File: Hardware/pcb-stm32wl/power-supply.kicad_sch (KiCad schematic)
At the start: 32 parts, among them J2 JST-PH, Q1 PMV32UP,215, Q3 PMV32UP,215, U11 MIC5365-3.3YD5, U12 TPS22917DBV, U8 MAX1837ETT50+T, U9 WE-TPC_5828

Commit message: review session 2
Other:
- note added: "ADD IN ANOTHER BATTERY"
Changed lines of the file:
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@@
-	)
-	(rectangle
-		(start 15.875 140.335)
-		(end 94.615 197.485)
-		(stroke
-			(width 0.508)
-			(type default)
-		)
-		(fill
-			(type none)
-		)
 	)
 	(rectangle
@@
 			)
 		)
+	)
+	(text "ADD IN ANOTHER BATTERY"
+		(exclude_from_sim no)
+		(at 130.048 18.034 0)
+		(effects
+			(font
+				(size 1.4986 1.4986)
+				(color 0 255 0 1)
+			)
+		)

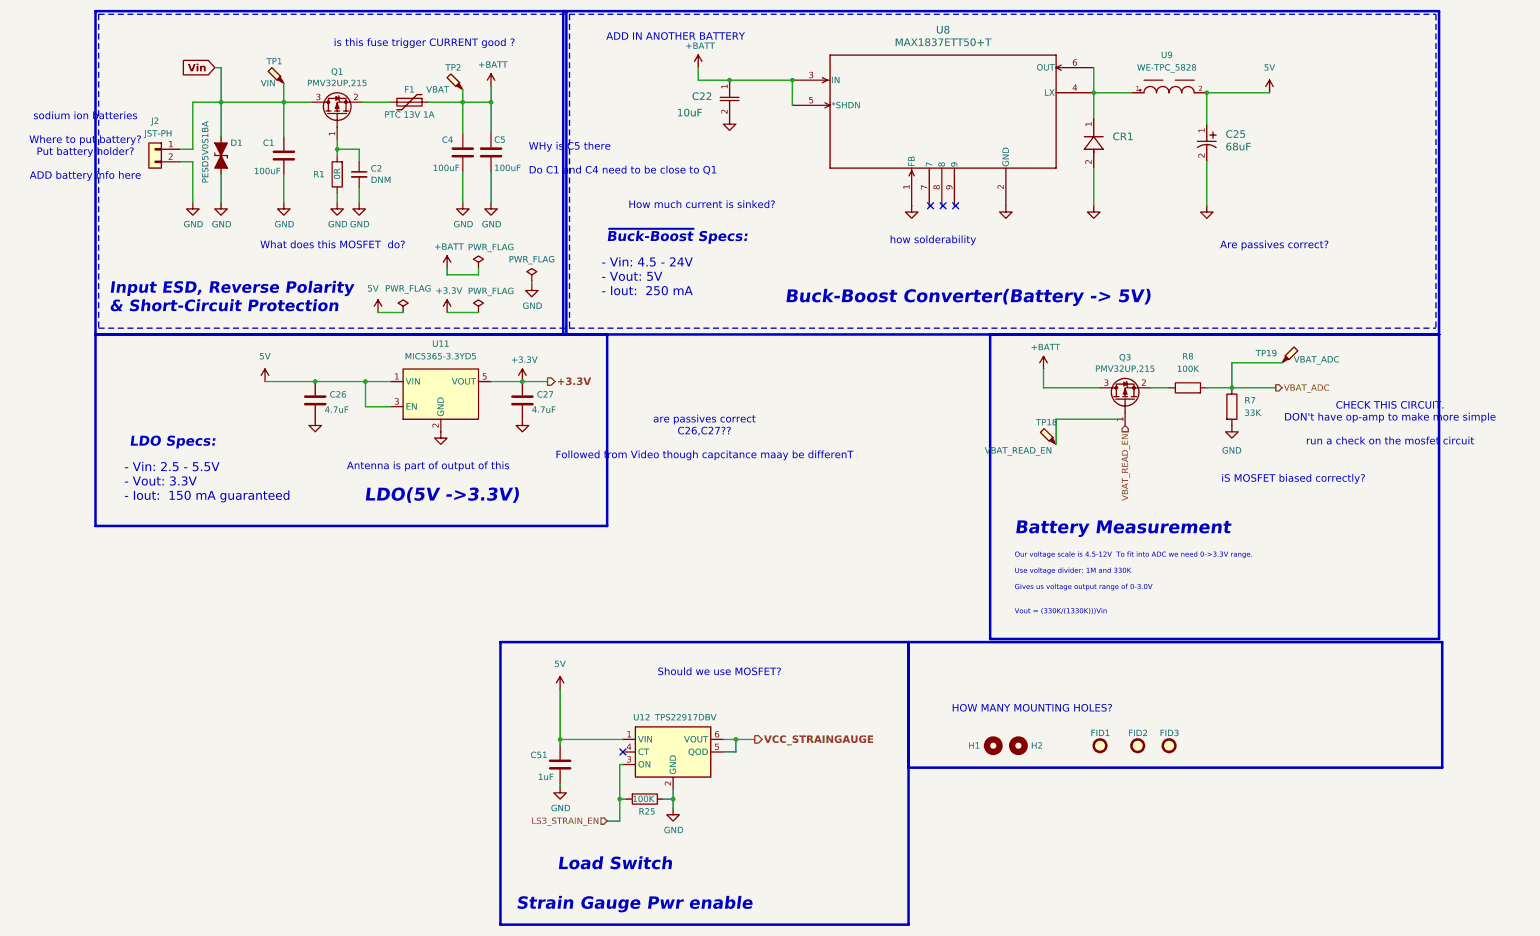
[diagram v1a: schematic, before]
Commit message: . Added NUCLEO reference schematics . Cleaned, renamed schematic pins for clarity . Fixed PMOS polarity bug . Added PMOS for switching StrainV . Added capacitors to AIN, StrainV . Cleaned git repository by removing backups, temporary lck files, ignoring KiCad cache files
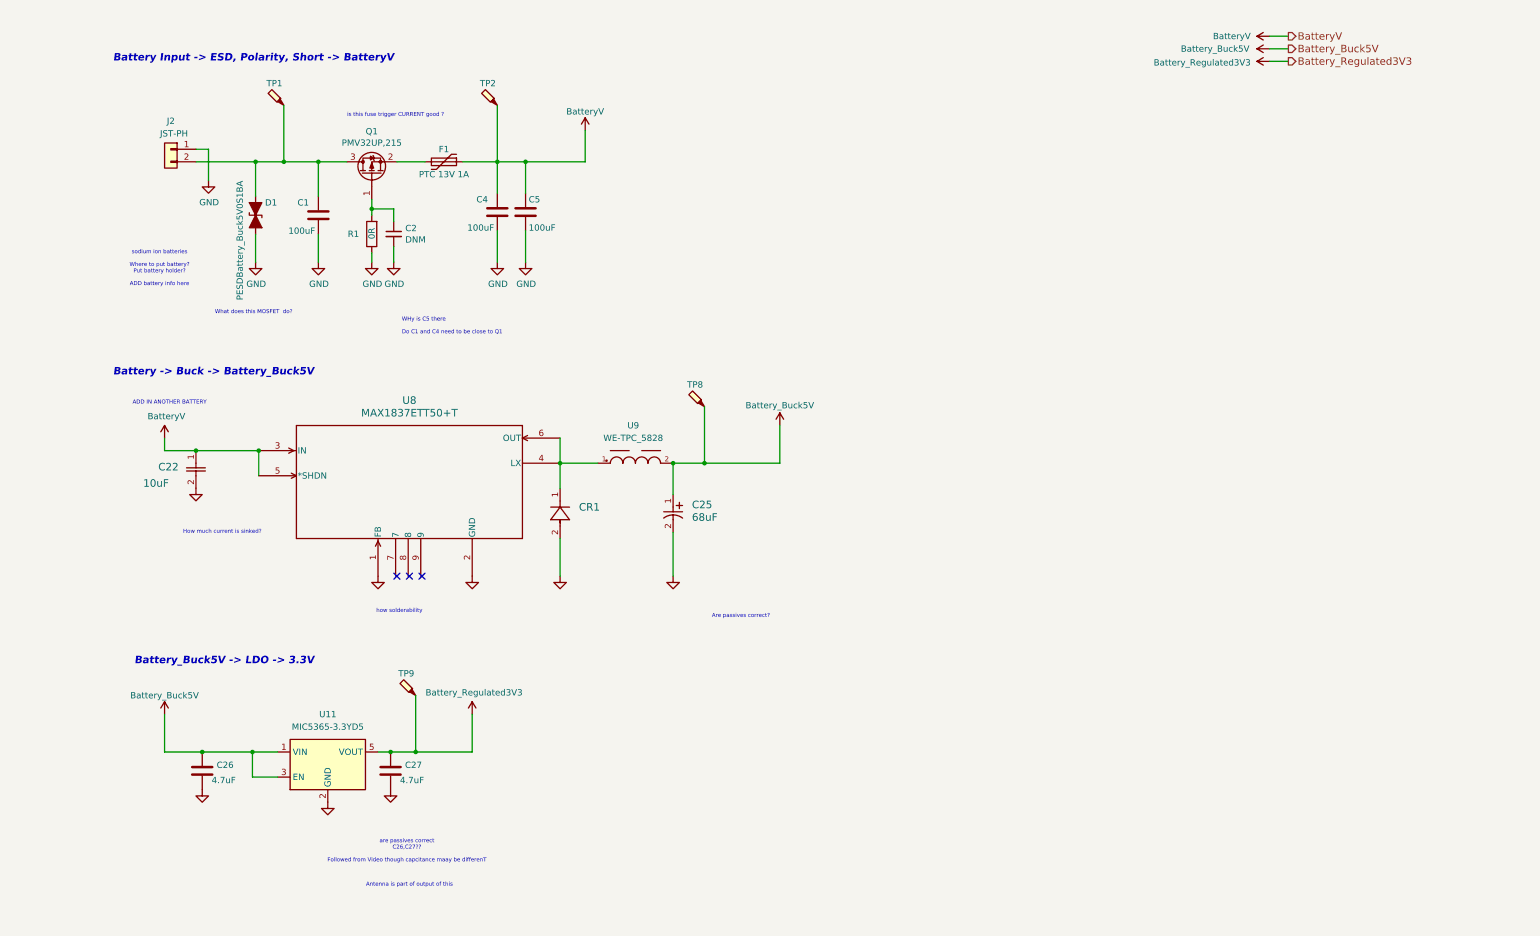
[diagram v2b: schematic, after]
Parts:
- removed C51: 1uF, Capacitor_SMD:C_0402_1005Metric, symbol Device:C
- removed FID1, FID2, FID3: Fiducial, Fiducial:Fiducial_1mm_Mask2mm, symbol Mechanical:Fiducial
- removed H1, H2: MountingHole, MountingHole:MountingHole_2.5mm, symbol Mechanical:MountingHole
- removed Q3: PMV32UP,215, Package_TO_SOT_SMD:SOT-23, symbol Device:Q_PMOS_GSD
- removed R25: 100K, Resistor_SMD:R_0402_1005Metric, symbol Device:R
- removed R7: 33K, symbol Device:R
- removed R8: 100K, symbol Device:R
- removed TP18: VBAT_READ_EN, TestPoint:TestPoint_Pad_D1.5mm, symbol Connector:TestPoint_Probe
- removed TP19: VBAT_ADC, TestPoint:TestPoint_Pad_D1.5mm, symbol Connector:TestPoint_Probe
- removed U12: TPS22917DBV, Package_TO_SOT_SMD:SOT-23-6, symbol Power_Management:TPS22917DBV
- added TP8, TP9: VBattery, TestPoint:TestPoint_Pad_D1.5mm, symbol Connector:TestPoint_Probe
- D1: value PESD5V0S1BA -> PESDBattery_Buck5V0S1BA
- TP1: value VIN -> VBattery_Unknown_Polarity
- TP2: value VBAT -> VBattery
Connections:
- net GND: now also J2.1 (Pin_1); no longer J2.2 (Pin_2)
- net +3.3V renamed Battery_Regulated3V3
- net Battery_Regulated3V3: now also TP9.1
- net +BATT renamed BatteryV
- net 5V renamed Battery_Buck5V
- net Battery_Buck5V: now also TP8.1
- net Vin: no longer names the net of C1.2, D1.1 (A1), Q1.3 (D), TP1.1
- net Vin: now also J2.2 (Pin_2); no longer J2.1 (Pin_1)
- no-connect marks 4 -> 3
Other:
- note added: "Battery -> Buck -> Battery_Buck5V"
- note added: "Battery Input -> ESD, Polarity, Short -> BatteryV"
- note added: "Battery_Buck5V -> LDO -> 3.3V"
- note removed: "- Vin: 2.5 - 5.5V - Vout: 3.3V - Iout: 150 mA guaranteed"
- note removed: "- Vin: 4.5 - 24V - Vout: 5V - Iout: 250 mA"
- note removed: "Battery Measurement"
- note removed: "Buck-Boost Converter(Battery -> 5V)"
- note removed: "CHECK THIS CIRCUIT. DON't have op-amp to make more simple run a check on the mosfet circuit"
- note removed: "HOW MANY MOUNTING HOLES?"
- note removed: "Input ESD, Reverse Polarity & Short-Circuit Protection"
- note removed: "LDO Specs:"
- note removed: "LDO(5V ->3.3V)"
- note removed: "Load Switch Strain Gauge Pwr enable"
- note removed: "Our voltage scale is 4.5-12V To fit into ADC we need 0->3.3V range. Use voltage divider: 1M and 330K Gives us voltage output range of 0-3.0V Vout = (330K/(1330K)))Vin"
- note removed: "Should we use MOSFET?"
- note removed: "iS MOSFET biased correctly?"
- note removed: "~{Buck-Boost} Specs:"
- moved on the sheet: C1, C2, C22, C25, C26, C27, C4, C5, CR1, D1, F1, J2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

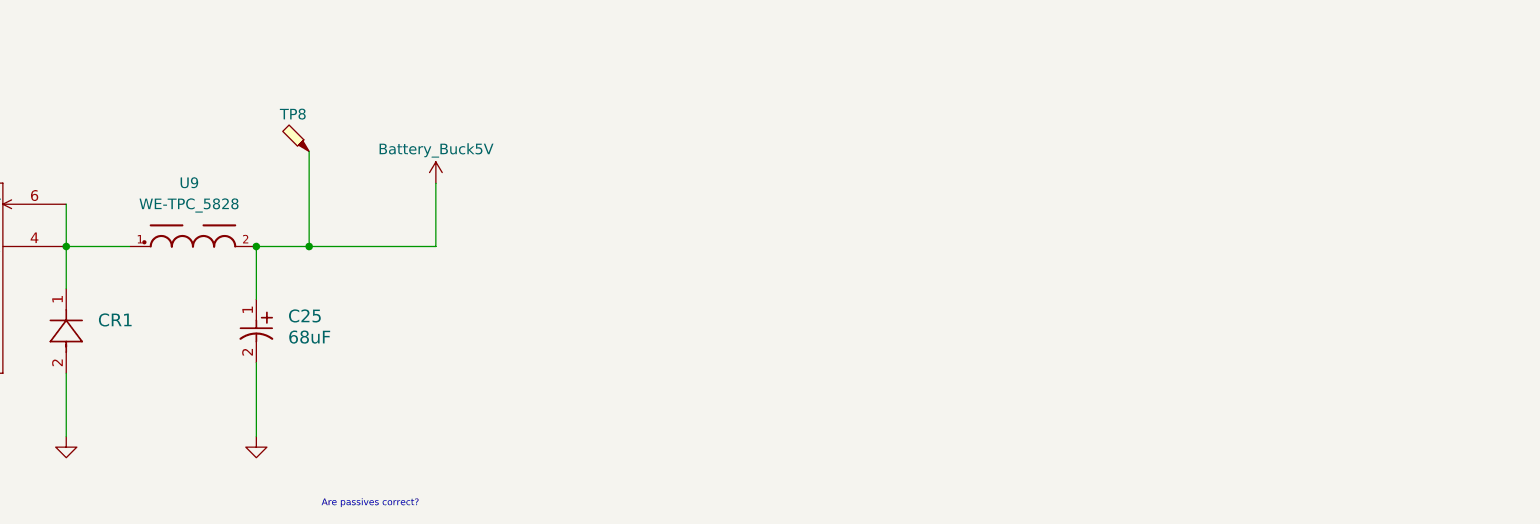
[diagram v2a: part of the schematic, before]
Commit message: Both mosfet will not be added into circuit. Both IMU and ANTENNA have sleep mode, which is in the micro to milliamp current usage range. Add in capacitor will optimize the system slighty, however the complexity of the problem is high. So I have opted to accept the uncertainty of the measurements.
Capacitor. Placement of capacitor is not accross differential. But we need 1 cap for each AIN, in addition to this, our switching frequency
will be varied significantly due to our battery range. This is very complicated stuff to size for. So in terms of time, it may be best to not add this in.
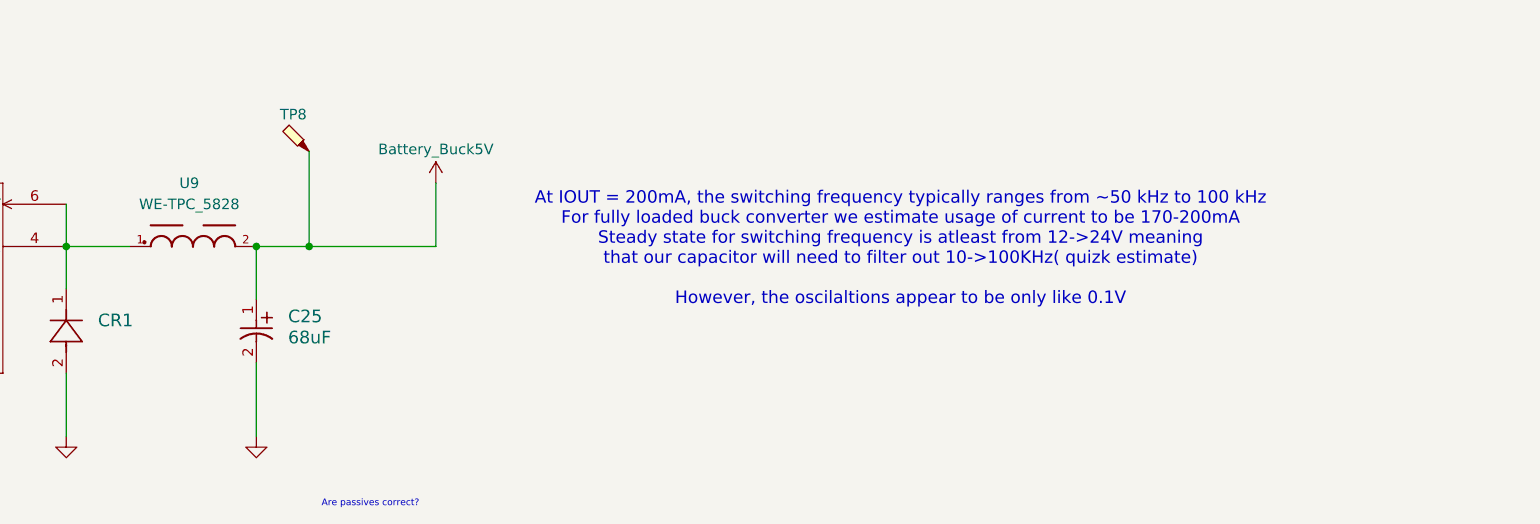
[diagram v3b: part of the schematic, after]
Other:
- note added: "At IOUT = 200mA, the switching frequency typically ranges from ~50 kHz to 100 kHz For fully loaded buck converter we estimate usage of current to be 170-200mA Steady state for switching frequency is atleast from 12->24V meaning that our capacitor will need to filter out 10->100KHz( quizk estimate) However, the oscilaltions appear to be only like 0.1V"
